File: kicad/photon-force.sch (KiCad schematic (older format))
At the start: 0 parts

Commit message: NeoPixel string in the schematic
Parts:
- added PH?: PHOTON, ~, symbol PHOTON
- added Q?: IRFML8244TRPBF, ~, symbol IRFML8244TRPBF
- added R?: GENERIC_RESISTOR, ~, symbol GENERIC_RESISTOR
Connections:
- net labels added: +3.3V, +5V
- wire segments 0 -> 4
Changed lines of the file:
@@
 LIBS:valves
 LIBS:parts
+LIBS:photon-force-cache
 EELAYER 27 0
 EELAYER END
 $Descr A4 11693 8268
 encoding utf-8
-Sheet 1 1
+Sheet 1 4
 Title ""
 Date "13 feb 2016"
@@
 Comment4 ""
 $EndDescr
+$Comp
+L PHOTON PH?
+U 1 1 56BF15F2
+P 5500 3900
+F 0 "PH?" H 5350 3250 60  0001 C CNN
+F 1 "PHOTON" V 5500 3900 60  0000 C CNN
+F 2 "~" H 5460 4060 60  0000 C CNN
+F 3 "~" H 5460 4060 60  0000 C CNN
+	1    5500 3900
+	1    0    0    -1
+$EndComp
+$Comp
+L IRFML8244TRPBF Q?
+U 1 1 56BF1634
+P 7100 4150
+F 0 "Q?" V 7250 4300 60  0000 C CNN
+F 1 "IRFML8244TRPBF" H 6350 3670 60  0001 C CNN
+F 2 "~" H 6300 4150 60  0000 C CNN
+F 3 "~" H 6300 4150 60  0000 C CNN
+	1    7100 4150
+	0    1    1    0
+$EndComp
+$Comp
+L +3.3V #PWR?
+U 1 1 56BF1657
+P 7050 3700
+F 0 "#PWR?" H 7050 3660 30  0001 C CNN
+F 1 "+3.3V" H 7050 3810 30  0000 C CNN
+F 2 "" H 7050 3700 60  0000 C CNN
+F 3 "" H 7050 3700 60  0000 C CNN
+	1    7050 3700
+	1    0    0    -1
+$EndComp
+$Comp
+L +5V #PWR?
+U 1 1 56BF1668
+P 7400 3700
+F 0 "#PWR?" H 7400 3790 20  0001 C CNN
+F 1 "+5V" H 7400 3790 30  0000 C CNN
+F 2 "" H 7400 3700 60  0000 C CNN
+F 3 "" H 7400 3700 60  0000 C CNN
+	1    7400 3700
+	1    0    0    -1
+$EndComp
+Wire Wire Line
+	6050 4150 6800 4150
+Wire Wire Line
+	7050 3700 7050 3850
+$Comp
+L GENERIC_RESISTOR R?
+U 1 1 56BF177E
+P 7400 3900
+F 0 "R?" H 7410 3780 60  0000 C CNN
+F 1 "GENERIC_RESISTOR" H 7440 3680 60  0001 C CNN
+F 2 "~" H 7350 3650 60  0000 C CNN
+F 3 "~" H 7350 3650 60  0000 C CNN
+	1    7400 3900
+	0    -1   -1   0
+$EndComp
+Wire Wire Line
+	7400 4100 7400 4150
+Wire Wire Line
+	7400 4150 7650 4150
+$Sheet
+S 8600 2350 1200 1050
+U 56BF0E3B
+F0 "Sensor Pod (chest)" 50
+F1 "sensorpod.sch" 50
+$EndSheet
+$Sheet
+S 1600 1500 1700 1350
+U 56BF0EB9
+F0 "Gun" 50
+F1 "gun.sch" 50
+$EndSheet
+$Sheet
+S 8650 3850 1200 1050
+U 56BF2119
+F0 "Sensor Pod (back)" 50
+F1 "sensorpod.sch" 50
+$EndSheet
 $EndSCHEMATC

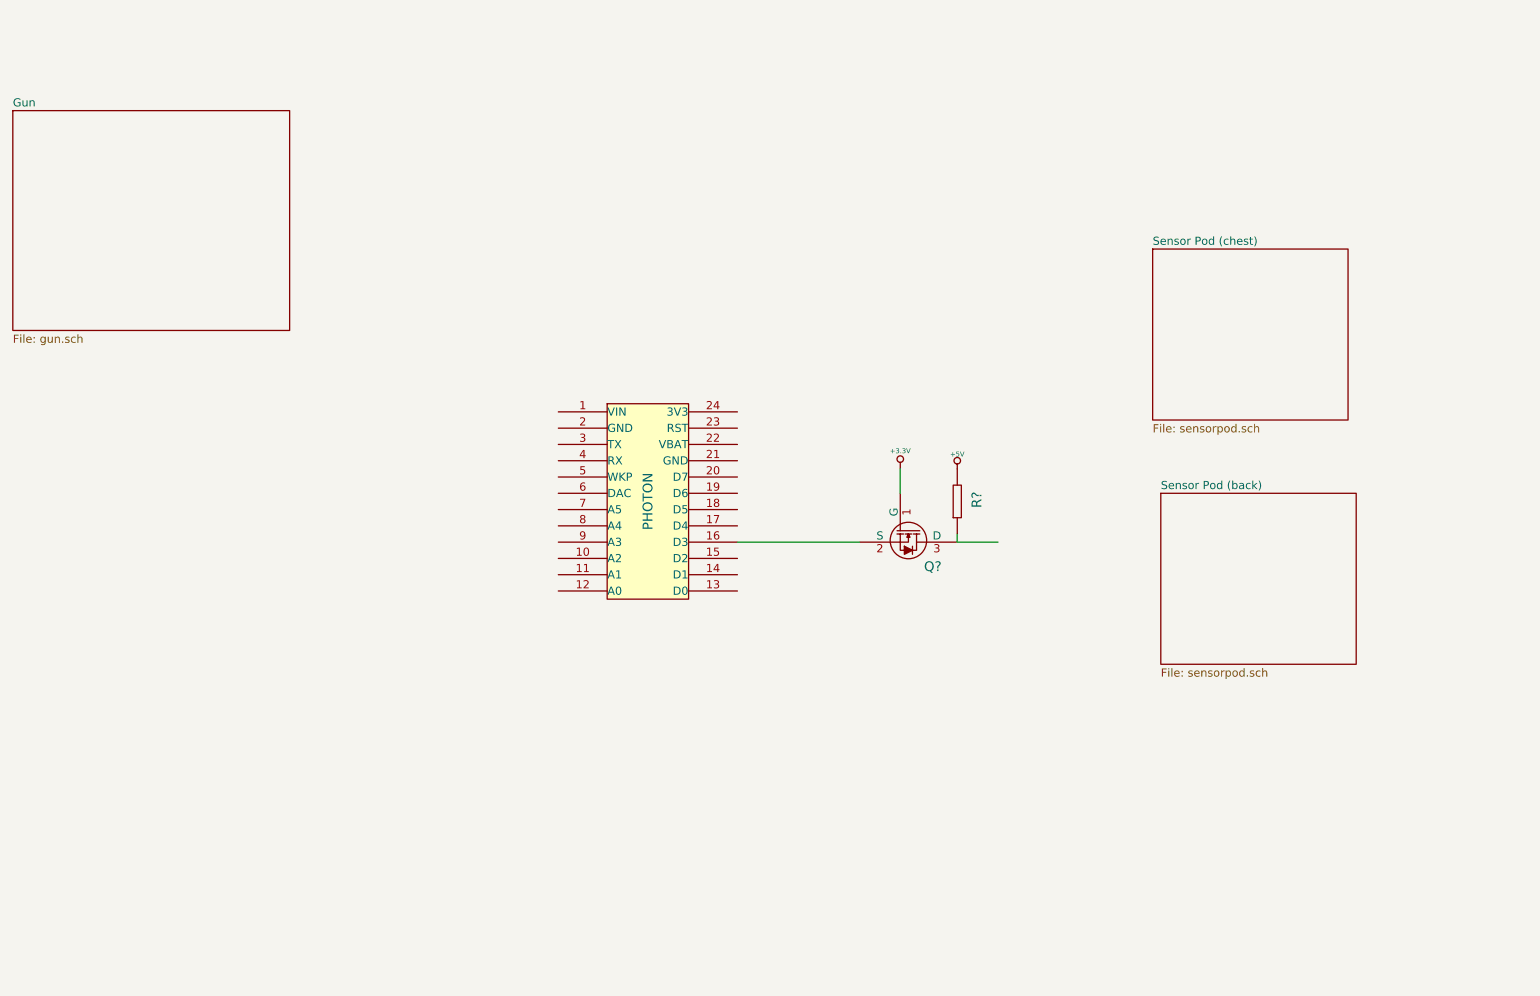
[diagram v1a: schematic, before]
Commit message: Sensor pos schematic done
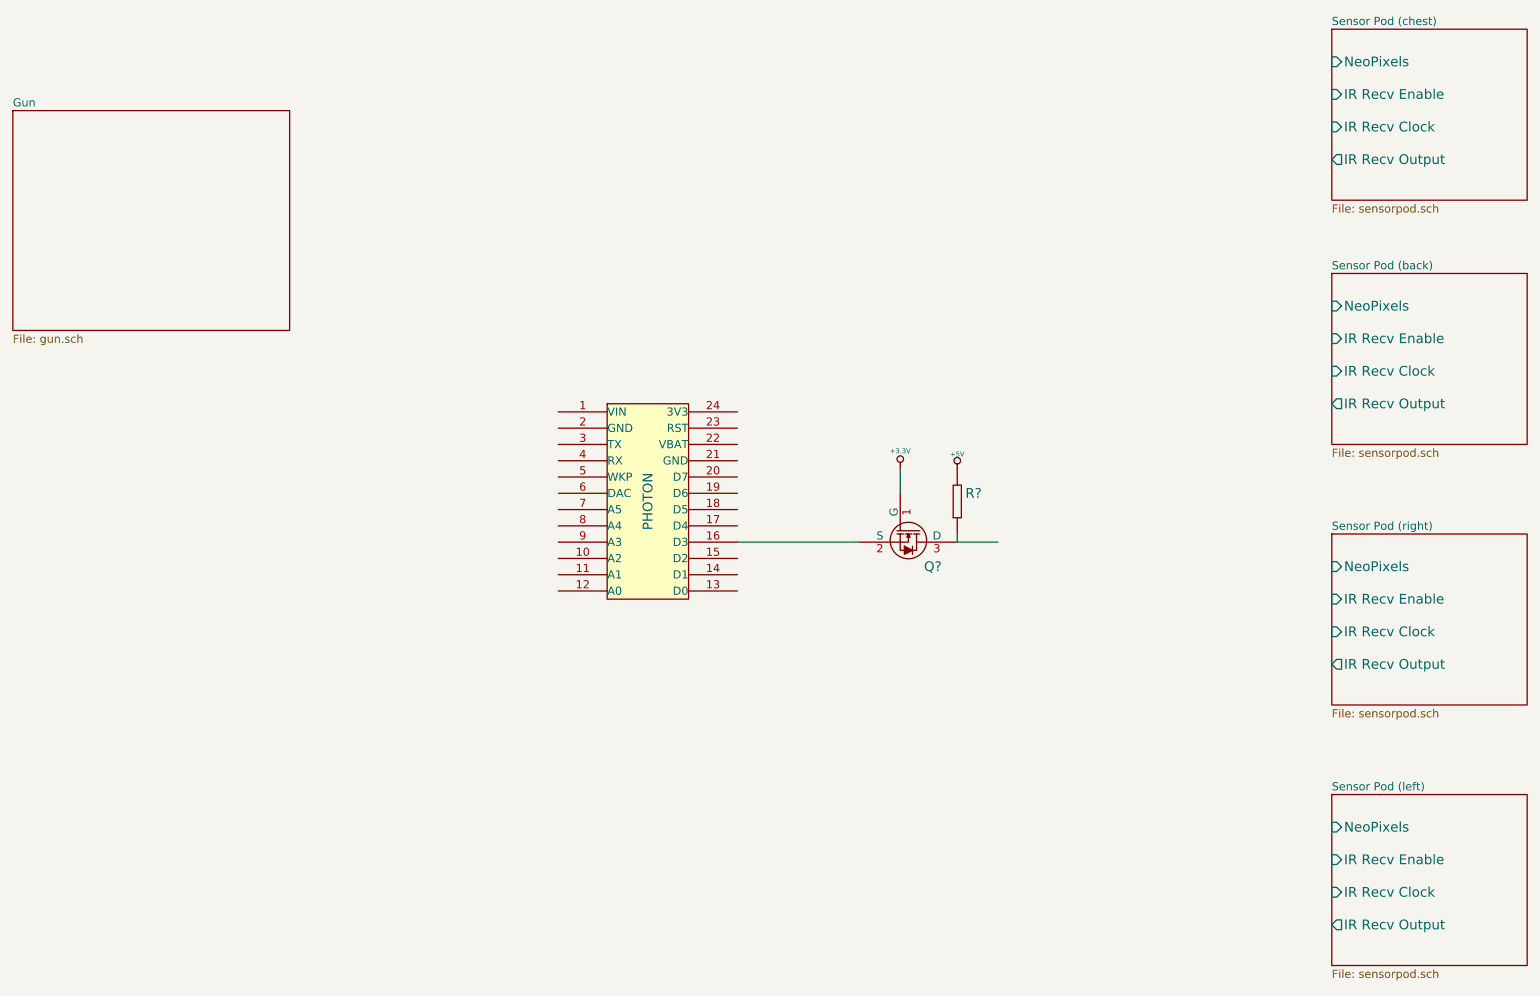
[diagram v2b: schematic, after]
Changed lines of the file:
@@
 Sheet 1 4
 Title ""
-Date "13 feb 2016"
+Date "16 feb 2016"
 Rev ""
 Comp ""
@@
 U 1 1 56BF177E
 P 7400 3900
-F 0 "R?" H 7410 3780 60  0000 C CNN
+F 0 "R?" V 7450 3800 60  0000 C CNN
 F 1 "GENERIC_RESISTOR" H 7440 3680 60  0001 C CNN
 F 2 "~" H 7350 3650 60  0000 C CNN
@@
 	7400 4150 7650 4150
 $Sheet
-S 8600 2350 1200 1050
-U 56BF0E3B
-F0 "Sensor Pod (chest)" 50
-F1 "sensorpod.sch" 50
-$EndSheet
-$Sheet
 S 1600 1500 1700 1350
 U 56BF0EB9
@@
 $EndSheet
 $Sheet
-S 8650 3850 1200 1050
+S 9700 2500 1200 1050
 U 56BF2119
 F0 "Sensor Pod (back)" 50
 F1 "sensorpod.sch" 50
+F2 "NeoPixels" I L 9700 2700 60
+F3 "IR Recv Enable" I L 9700 2900 60
+F4 "IR Recv Clock" I L 9700 3100 60
+F5 "IR Recv Output" O L 9700 3300 60
+$EndSheet
+$Sheet
+S 9700 1000 1200 1050
+U 56BF0E3B
+F0 "Sensor Pod (chest)" 50
+F1 "sensorpod.sch" 50
+F2 "NeoPixels" I L 9700 1200 60
+F3 "IR Recv Enable" I L 9700 1400 60
+F4 "IR Recv Clock" I L 9700 1600 60
+F5 "IR Recv Output" O L 9700 1800 60
+$EndSheet
+$Sheet
+S 9700 5700 1200 1050
+U 56C34A19
+F0 "Sensor Pod (left)" 50
+F1 "sensorpod.sch" 50
+F2 "NeoPixels" I L 9700 5900 60
+F3 "IR Recv Enable" I L 9700 6100 60
+F4 "IR Recv Clock" I L 9700 6300 60
+F5 "IR Recv Output" O L 9700 6500 60
+$EndSheet
+$Sheet
+S 9700 4100 1200 1050
+U 56C34E98
+F0 "Sensor Pod (right)" 50
+F1 "sensorpod.sch" 50
+F2 "NeoPixels" I L 9700 4300 60
+F3 "IR Recv Enable" I L 9700 4500 60
+F4 "IR Recv Clock" I L 9700 4700 60
+F5 "IR Recv Output" O L 9700 4900 60
 $EndSheet
 $EndSCHEMATC
